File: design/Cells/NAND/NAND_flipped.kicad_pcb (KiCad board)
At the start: 2 copper layers, 4 parts, among them P1 Q_PJFET_GSD, P2 Q_PJFET_GSD

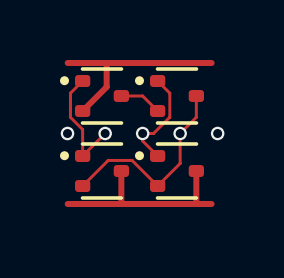
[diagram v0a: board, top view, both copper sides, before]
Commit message: All gates layout on a strict 2.5mm grid. Flipped versions of all three layouts
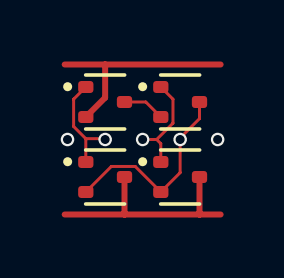
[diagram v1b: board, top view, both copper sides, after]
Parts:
- moved P1 0.23 mm to (1.25, 3.75)
- moved P2 0.23 mm to (3.75, 3.75)
- moved N1 0.23 mm to (1.25, 1.25)
- moved N2 0.23 mm to (3.75, 1.25)
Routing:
- net VDD: track 7.01 -> 7.70 mm
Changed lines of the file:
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@@
 	(footprint "Package_TO_SOT_SMD:SOT-523"
 		(layer "F.Cu")
-		(at 3.645 1.05)
+		(at 3.75 1.25)
 		(descr "SOT523, https://www.diodes.com/assets/Package-Files/SOT523.pdf")
 		(tags "SOT-523")
@@
 	(footprint "Package_TO_SOT_SMD:SOT-523"
 		(layer "F.Cu")
-		(at 3.645 3.55)
+		(at 3.75 3.75)
 		(descr "SOT523, https://www.diodes.com/assets/Package-Files/SOT523.pdf")
 		(tags "SOT-523")
@@
 	(footprint "Package_TO_SOT_SMD:SOT-523"
 		(layer "F.Cu")
-		(at 1.145 1.05)
+		(at 1.25 1.25)
 		(descr "SOT523, https://www.diodes.com/assets/Package-Files/SOT523.pdf")
 		(tags "SOT-523")
@@
 	(footprint "Package_TO_SOT_SMD:SOT-523"
 		(layer "F.Cu")
-		(at 1.145 3.55)
+		(at 1.25 3.75)
 		(descr "SOT523, https://www.diodes.com/assets/Package-Files/SOT523.pdf")
 		(tags "SOT-523")
@@
 	)
 	(via
-		(at 5 2.3)
+		(at 5 2.5)
 		(size 0.45)
 		(drill 0.3)
@@
 	)
 	(via
-		(at -0.005 2.3)
+		(at -0.005 2.5)
 		(size 0.45)
 		(drill 0.3)
@@
 	)
 	(segment
-		(start 1.351 3.199)
-		(end 0.5 4.05)
+		(start 3.75 2.5)
+		(end 3.75 2.45)
 		(width 0.1)
 		(layer "F.Cu")
@@
 	)
 	(segment
-		(start 3.75 3.3)
-		(end 3 4.05)
+		(start 4.395 1.805)
+		(end 4.395 1.25)
 		(width 0.1)
 		(layer "F.Cu")
@@
 	)
 	(segment
-		(start 2.149 3.199)
-		(end 1.351 3.199)
+		(start 2.254 3.399)
+		(end 3.105 4.25)
 		(width 0.1)
 		(layer "F.Cu")
@@
 	)
 	(segment
-		(start 4.29 1.76)
-		(end 3.75 2.3)
+		(start 1.456 3.399)
+		(end 2.254 3.399)
 		(width 0.1)
 		(layer "F.Cu")
@@
 	)
 	(segment
-		(start 3 4.05)
-		(end 2.149 3.199)
+		(start 3.105 4.25)
+		(end 3.75 3.605)
 		(width 0.1)
 		(layer "F.Cu")
@@
 	)
 	(segment
-		(start 4.29 1.05)
-		(end 4.29 1.76)
+		(start 3.75 3.605)
+		(end 3.75 2.5)
 		(width 0.1)
 		(layer "F.Cu")
@@
 	)
 	(segment
-		(start 3.75 2.3)
-		(end 3.75 3.3)
+		(start 3.75 2.45)
+		(end 4.395 1.805)
 		(width 0.1)
 		(layer "F.Cu")
 		(net 1)
 	)
+	(segment
+		(start 0.605 4.25)
+		(end 1.456 3.399)
+		(width 0.1)
+		(layer "F.Cu")
+		(net 1)
+	)
 	(via
-		(at 3.75 2.3)
+		(at 3.75 2.5)
 		(size 0.45)
 		(drill 0.3)
@@
 	)
 	(segment
-		(start 0.5 1.55)
-		(end 1.3 0.75)
+		(start 1.25 1.105)
+		(end 1.25 0)
 		(width 0.2)
 		(layer "F.Cu")
@@
 	)
 	(segment
-		(start 4.3 -0.05)
-		(end 4.8 -0.05)
+		(start 1.25 0)
+		(end 5.1 0)
 		(width 0.2)
 		(layer "F.Cu")
@@
 	)
 	(segment
-		(start 1.3 0.75)
-		(end 1.3 -0.05)
+		(start -0.1 0)
+		(end 1.25 0)
 		(width 0.2)
 		(layer "F.Cu")
@@
 	)
 	(segment
-		(start 1.15 -0.05)
-		(end 0 -0.05)
+		(start 0.605 1.75)
+		(end 1.25 1.105)
 		(width 0.2)
 		(layer "F.Cu")
@@
 	)
 	(segment
-		(start 1.8 -0.05)
-		(end 4.3 -0.05)
-		(width 0.2)
-		(layer "F.Cu")
-		(net 2)
-	)
-	(segment
-		(start 1.8 -0.05)
-		(end 1.3 -0.05)
-		(width 0.2)
-		(layer "F.Cu")
-		(net 2)
-	)
-	(segment
-		(start 1.3 -0.05)
-		(end 1.15 -0.05)
-		(width 0.2)
-		(layer "F.Cu")
-		(net 2)
-	)
-	(segment
-		(start 0.094 1.761189)
-		(end 0.5 2.167189)
+		(start 0.605 2.472189)
+		(end 1.222189 2.472189)
 		(width 0.1)
 		(layer "F.Cu")
@@
 	)
 	(segment
-		(start 0.5 3.05)
-		(end 1.25 2.3)
+		(start 1.222189 2.472189)
+		(end 1.25 2.5)
 		(width 0.1)
 		(layer "F.Cu")
@@
 	)
 	(segment
-		(start 0.5 2.167189)
-		(end 0.5 3.05)
+		(start 0.199 2.066189)
+		(end 0.605 2.472189)
 		(width 0.1)
 		(layer "F.Cu")
@@
 	)
 	(segment
-		(start 0.094 0.956)
-		(end 0.094 1.761189)
+		(start 0.199 1.156)
+		(end 0.199 2.066189)
 		(width 0.1)
 		(layer "F.Cu")
@@
 	)
 	(segment
-		(start 0.5 0.55)
-		(end 0.094 0.956)
+		(start 0.605 0.75)
+		(end 0.199 1.156)
 		(width 0.1)
 		(layer "F.Cu")
 		(net 3)
 	)
+	(segment
+		(start 0.605 2.472189)
+		(end 0.605 3.25)
+		(width 0.1)
+		(layer "F.Cu")
+		(net 3)
+	)
 	(via
-		(at 1.25 2.3)
+		(at 1.25 2.5)
 		(size 0.45)
 		(drill 0.3)
@@
 	)
 	(segment
-		(start 1.79 3.55)
-		(end 1.79 4.64)
+		(start -0.1 5)
+		(end 1.9 5)
 		(width 0.2)
 		(layer "F.Cu")
@@
 	)
 	(segment
-		(start 1.79 4.64)
-		(end 1.8 4.65)
-		(width 0.1)
+		(start 4.4 5)
+		(end 5.1 5)
+		(width 0.2)
 		(layer "F.Cu")
 		(net 4)
 	)
 	(segment
-		(start 4.29 3.55)
-		(end 4.29 4.64)
+		(start 1.9 5)
+		(end 4.4 5)
 		(width 0.2)
 		(layer "F.Cu")
@@
 	)
 	(segment
-		(start 4.29 4.64)
-		(end 4.3 4.65)
-		(width 0.1)
+		(start 1.895 4.995)
+		(end 1.9 5)
+		(width 0.2)
 		(layer "F.Cu")
 		(net 4)
 	)
 	(segment
-		(start 0.5 4.65)
-		(end 0 4.65)
+		(start 4.395 3.75)
+		(end 4.395 4.995)
 		(width 0.2)
 		(layer "F.Cu")
@@
 	)
 	(segment
-		(start 4.3 4.65)
-		(end 4.8 4.65)
+		(start 4.395 4.995)
+		(end 4.4 5)
 		(width 0.2)
 		(layer "F.Cu")
@@
 	)
 	(segment
-		(start 1.8 4.65)
-		(end 4.3 4.65)
+		(start 1.895 3.75)
+		(end 1.895 4.995)
 		(width 0.2)
 		(layer "F.Cu")
@@
 	)
 	(segment
-		(start 0.5 4.65)
-		(end 1.8 4.65)
-		(width 0.2)
-		(layer "F.Cu")
-		(net 4)
-	)
-	(segment
-		(start 1.79 1.05)
-		(end 2.5 1.05)
+		(start 1.895 1.25)
+		(end 2.605 1.25)
 		(width 0.1)
 		(layer "F.Cu")
@@
 	)
 	(segment
-		(start 2.5 1.05)
-		(end 3 1.55)
+		(start 2.605 1.25)
+		(end 3.105 1.75)
 		(width 0.1)
 		(layer "F.Cu")
@@
 	)
 	(segment
-		(start 3 0.55)
-		(end 3.406 0.956)
+		(start 3.105 2.637262)
+		(end 2.967738 2.5)
 		(width 0.1)
 		(layer "F.Cu")
@@
 	)
 	(segment
-		(start 2.5 2.3)
-		(end 2.5 2.55)
+		(start 3.105 3.25)
+		(end 3.105 2.637262)
 		(width 0.1)
 		(layer "F.Cu")
@@
 	)
 	(segment
-		(start 2.5 2.55)
-		(end 3 3.05)
+		(start 3.511 1.956738)
+		(end 2.967738 2.5)
 		(width 0.1)
 		(layer "F.Cu")
@@
 	)
 	(segment
-		(start 3.406 0.956)
-		(end 3.406 1.756738)
+		(start 3.511 1.156)
+		(end 3.511 1.956738)
 		(width 0.1)
 		(layer "F.Cu")
@@
 	)
 	(segment
-		(start 3.406 1.756738)
-		(end 2.862738 2.3)
+		(start 3.105 0.75)
+		(end 3.511 1.156)
 		(width 0.1)
 		(layer "F.Cu")
@@
 	)
 	(segment
-		(start 2.862738 2.3)
-		(end 2.5 2.3)
+		(start 2.967738 2.5)
+		(end 2.5 2.5)
 		(width 0.1)
 		(layer "F.Cu")
@@
 	)
 	(via
-		(at 2.5 2.3)
+		(at 2.5 2.5)
 		(size 0.45)
 		(drill 0.3)

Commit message: flip the cells to share power lines
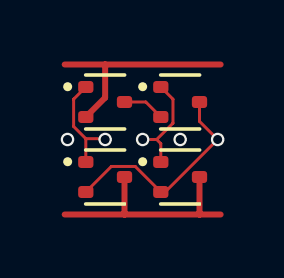
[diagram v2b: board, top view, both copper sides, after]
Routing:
- net Y: track 6.74 -> 7.33 mm
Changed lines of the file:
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@@
 	)
 	(via
-		(at 5 2.5)
+		(at 3.75 2.5)
 		(size 0.45)
 		(drill 0.3)
@@
 	)
 	(segment
-		(start 3.75 2.5)
-		(end 3.75 2.45)
+		(start 4.395 1.895)
+		(end 4.395 1.25)
 		(width 0.1)
 		(layer "F.Cu")
@@
 	)
 	(segment
-		(start 4.395 1.805)
-		(end 4.395 1.25)
+		(start 3.25 4.25)
+		(end 5 2.5)
+		(width 0.1)
+		(layer "F.Cu")
+		(net 1)
+	)
+	(segment
+		(start 5 2.5)
+		(end 4.395 1.895)
 		(width 0.1)
 		(layer "F.Cu")
@@
 	(segment
 		(start 3.105 4.25)
-		(end 3.75 3.605)
-		(width 0.1)
-		(layer "F.Cu")
-		(net 1)
-	)
-	(segment
-		(start 3.75 3.605)
-		(end 3.75 2.5)
-		(width 0.1)
-		(layer "F.Cu")
-		(net 1)
-	)
-	(segment
-		(start 3.75 2.45)
-		(end 4.395 1.805)
+		(end 3.25 4.25)
 		(width 0.1)
 		(layer "F.Cu")
@@
 	)
 	(via
-		(at 3.75 2.5)
+		(at 5 2.5)
 		(size 0.45)
 		(drill 0.3)
